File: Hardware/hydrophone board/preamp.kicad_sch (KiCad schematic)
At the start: 10 parts, among them U111 AD8541ARTZ

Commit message: changed all cap + resistors to 0805, starting filter layout
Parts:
- C111, C112, C114: footprint Capacitor_SMD:C_0603_1608Metric -> Capacitor_SMD:C_0805_2012Metric_Pad1.18x1.45mm_HandSolder
- C113: footprint Capacitor_SMD:C_0805_2012Metric -> Capacitor_SMD:C_0805_2012Metric_Pad1.18x1.45mm_HandSolder
- R111, R112, R113, R114: footprint Resistor_SMD:R_0603_1608Metric -> Resistor_SMD:R_0805_2012Metric_Pad1.20x1.40mm_HandSolder
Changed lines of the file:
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@@
       (effects (font (size 1.27 1.27)))
     )
-    (property "Footprint" "Capacitor_SMD:C_0603_1608Metric" (at 120.65 64.4652 0)
+    (property "Footprint" "Capacitor_SMD:C_0805_2012Metric_Pad1.18x1.45mm_HandSolder" (at 120.65 64.4652 0)
       (effects (font (size 1.27 1.27)) hide)
     )
@@
       (effects (font (size 1.27 1.27)) (justify left))
     )
-    (property "Footprint" "Resistor_SMD:R_0603_1608Metric" (at 96.266 108.204 90)
+    (property "Footprint" "Resistor_SMD:R_0805_2012Metric_Pad1.20x1.40mm_HandSolder" (at 96.266 108.204 90)
       (effects (font (size 1.27 1.27)) hide)
     )
@@
       (effects (font (size 1.27 1.27)))
     )
-    (property "Footprint" "Resistor_SMD:R_0603_1608Metric" (at 124.714 75.184 90)
+    (property "Footprint" "Resistor_SMD:R_0805_2012Metric_Pad1.20x1.40mm_HandSolder" (at 124.714 75.184 90)
       (effects (font (size 1.27 1.27)) hide)
     )
@@
       (effects (font (size 1.27 1.27)))
     )
-    (property "Footprint" "Capacitor_SMD:C_0805_2012Metric" (at 86.36 85.3948 0)
+    (property "Footprint" "Capacitor_SMD:C_0805_2012Metric_Pad1.18x1.45mm_HandSolder" (at 86.36 85.3948 0)
       (effects (font (size 1.27 1.27)) hide)
     )
@@
       (effects (font (size 1.27 1.27)) (justify right))
     )
-    (property "Footprint" "Capacitor_SMD:C_0603_1608Metric" (at 106.9848 116.84 0)
+    (property "Footprint" "Capacitor_SMD:C_0805_2012Metric_Pad1.18x1.45mm_HandSolder" (at 106.9848 116.84 0)
       (effects (font (size 1.27 1.27)) hide)
     )
@@
       (effects (font (size 1.27 1.27)))
     )
-    (property "Footprint" "Capacitor_SMD:C_0603_1608Metric" (at 130.81 49.8348 0)
+    (property "Footprint" "Capacitor_SMD:C_0805_2012Metric_Pad1.18x1.45mm_HandSolder" (at 130.81 49.8348 0)
       (effects (font (size 1.27 1.27)) hide)
     )
@@
       (effects (font (size 1.27 1.27)) (justify right))
     )
-    (property "Footprint" "Resistor_SMD:R_0603_1608Metric" (at 62.484 78.486 90)
+    (property "Footprint" "Resistor_SMD:R_0805_2012Metric_Pad1.20x1.40mm_HandSolder" (at 62.484 78.486 90)
       (effects (font (size 1.27 1.27)) hide)
     )
@@
       (effects (font (size 1.27 1.27)) (justify left))
     )
-    (property "Footprint" "Resistor_SMD:R_0603_1608Metric" (at 96.266 120.904 90)
-      (effects (font (size 1.27 1.27)) hide)
-    )
+    (property "Footprint" "Resistor_SMD:R_0805_2012Metric_Pad1.20x1.40mm_HandSolder" (at 96.266 120.904 90)
+      (effects (font (size 1.27 1.27)) hide)
+    )

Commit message: changed some aprts
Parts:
- removed TP?: TestPoint_Probe, Connector_PinHeader_2.54mm:PinHeader_1x01_P2.54mm_Vertical, symbol Connector:TestPoint_Probe
- added J5: Conn_01x02, Connector_PinHeader_2.54mm:PinHeader_1x02_P2.54mm_Vertical, symbol Connector_Generic:Conn_01x02
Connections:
- net GND: now also J5.1 (Pin_1)
- net OUT: now also J5.2 (Pin_2)
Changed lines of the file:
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@@
+    (stroke (width 0) (type default))
+  )
+  (wire (pts (xy 146.05 88.9) (xy 146.05 99.06))
     (stroke (width 0) (type default))
   )
@@
     (stroke (width 0) (type default))
   )
-  (wire (pts (xy 146.05 82.55) (xy 146.05 88.9))
+  (wire (pts (xy 146.05 101.6) (xy 146.05 106.68))
     (stroke (width 0) (type default))
   )
@@
     )
   )
+  (symbol (lib_id "power:GND") (at 146.05 106.68 0) (unit 1)
+    (in_bom yes) (on_board yes) (dnp no) (fields_autoplaced)
+    (property "Reference" "#PWR0205" (at 146.05 113.03 0)
+      (effects (font (size 1.27 1.27)) hide)
+    )
+    (property "Value" "GND" (at 146.05 111.76 0)
+      (effects (font (size 1.27 1.27)))
+    )
+    (property "Footprint" "" (at 146.05 106.68 0)
+      (effects (font (size 1.27 1.27)) hide)
+    )
+    (property "Datasheet" "" (at 146.05 106.68 0)
+      (effects (font (size 1.27 1.27)) hide)
+    )
+    (pin "1")
+    (instances
+      (project "hydrophone board"
+        (path "/4356d3a6-6a00-447d-897e-473f60221539/1cfbaf71-7039-4355-8fc7-d8c77f0e8058"
+          (reference "#PWR0205") (unit 1)
+        )
+        (path "/4356d3a6-6a00-447d-897e-473f60221539/f560d530-135c-40dc-9144-4f9599a30f13"
+          (reference "#PWR0252") (unit 1)
+        )
+        (path "/4356d3a6-6a00-447d-897e-473f60221539/fa1a46a1-ed86-4a84-a182-b5dbe7fc86e7"
+          (reference "#PWR0253") (unit 1)
+        )
+        (path "/4356d3a6-6a00-447d-897e-473f60221539/d3a562a3-af99-4bb5-b5fa-eb83660cffa4"
+          (reference "#PWR0254") (unit 1)
+        )
+        (path "/4356d3a6-6a00-447d-897e-473f60221539/6f981a72-1f6f-4ccf-ba7d-c5dfb70b4229"
+          (reference "#PWR0255") (unit 1)
+        )
+      )
+    )
+  )
   (symbol (lib_id "Device:C") (at 127 50.8 90) (unit 1)
     (in_bom yes) (on_board yes) (dnp no) (fields_autoplaced)
@@
         (path "/4356d3a6-6a00-447d-897e-473f60221539/6f981a72-1f6f-4ccf-ba7d-c5dfb70b4229"
           (reference "C141") (unit 1)
-        )
-      )
-    )
-  )
-  (symbol (lib_id "Connector:TestPoint_Probe") (at 146.05 82.55 0) (unit 1)
-    (in_bom yes) (on_board yes) (dnp no) (fields_autoplaced)
-    (property "Reference" "TP?" (at 149.86 80.3275 0)
-      (effects (font (size 1.27 1.27)) (justify left))
-    )
-    (property "Value" "TestPoint_Probe" (at 149.86 82.8675 0)
-      (effects (font (size 1.27 1.27)) (justify left))
-    )
-    (property "Footprint" "Connector_PinHeader_2.54mm:PinHeader_1x01_P2.54mm_Vertical" (at 151.13 82.55 0)
-      (effects (font (size 1.27 1.27)) hide)
-    )
-    (property "Datasheet" "~" (at 151.13 82.55 0)
-      (effects (font (size 1.27 1.27)) hide)
-    )
-    (pin "1")
-    (instances
-      (project "hydrophone board"
-        (path "/4356d3a6-6a00-447d-897e-473f60221539/cf9d259f-9643-49eb-8aca-1ca8b75f4d64"
-          (reference "TP?") (unit 1)
-        )
-        (path "/4356d3a6-6a00-447d-897e-473f60221539/f560d530-135c-40dc-9144-4f9599a30f13"
-          (reference "TP111") (unit 1)
-        )
-        (path "/4356d3a6-6a00-447d-897e-473f60221539/fa1a46a1-ed86-4a84-a182-b5dbe7fc86e7"
-          (reference "TP121") (unit 1)
-        )
-        (path "/4356d3a6-6a00-447d-897e-473f60221539/d3a562a3-af99-4bb5-b5fa-eb83660cffa4"
-          (reference "TP131") (unit 1)
-        )
-        (path "/4356d3a6-6a00-447d-897e-473f60221539/6f981a72-1f6f-4ccf-ba7d-c5dfb70b4229"
-          (reference "TP141") (unit 1)
         )
       )
@@
         )
       )
+    )
+  )
+  (symbol (lib_id "Connector_Generic:Conn_01x02") (at 140.97 101.6 180) (unit 1)
+    (in_bom yes) (on_board yes) (dnp no)
+    (property "Reference" "J5" (at 140.97 92.71 0)
+      (effects (font (size 1.27 1.27)))
+    )
+    (property "Value" "Conn_01x02" (at 140.97 95.25 0)
+      (effects (font (size 1.27 1.27)))
+    )
+    (property "Footprint" "Connector_PinHeader_2.54mm:PinHeader_1x02_P2.54mm_Vertical" (at 140.97 101.6 0)
+      (effects (font (size 1.27 1.27)) hide)
+    )
+    (property "Datasheet" "~" (at 140.97 101.6 0)
+      (effects (font (size 1.27 1.27)) hide)
+    )
+    (pin "1")
+    (pin "2")
+    (instances
+      (project "hydrophone board"
+        (path "/4356d3a6-6a00-447d-897e-473f60221539/1cfbaf71-7039-4355-8fc7-d8c77f0e8058"
+          (reference "J5") (unit 1)
+        )
+        (path "/4356d3a6-6a00-447d-897e-473f60221539/f560d530-135c-40dc-9144-4f9599a30f13"
+          (reference "J111") (unit 1)
+        )
+        (path "/4356d3a6-6a00-447d-897e-473f60221539/fa1a46a1-ed86-4a84-a182-b5dbe7fc86e7"
+          (reference "J121") (unit 1)
+        )
+        (path "/4356d3a6-6a00-447d-897e-473f60221539/d3a562a3-af99-4bb5-b5fa-eb83660cffa4"
+          (reference "J131") (unit 1)
+        )
+        (path "/4356d3a6-6a00-447d-897e-473f60221539/6f981a72-1f6f-4ccf-ba7d-c5dfb70b4229"
+          (reference "J141") (unit 1)
+        )
+      )

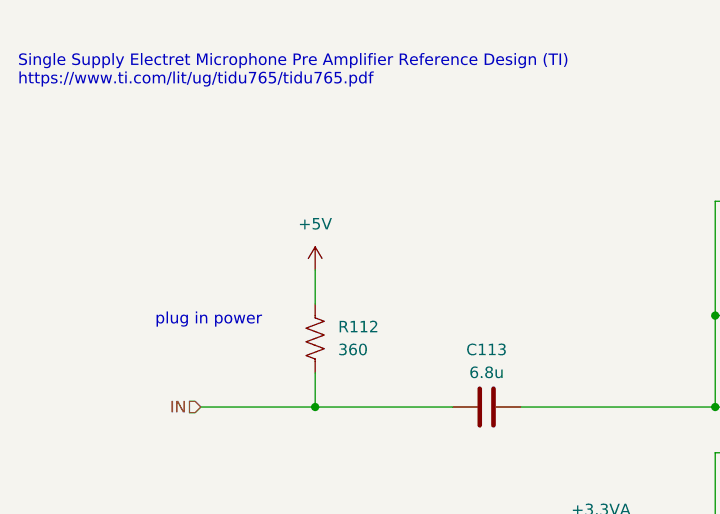
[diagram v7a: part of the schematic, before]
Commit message: power routing, changed bias voltage to 3.3
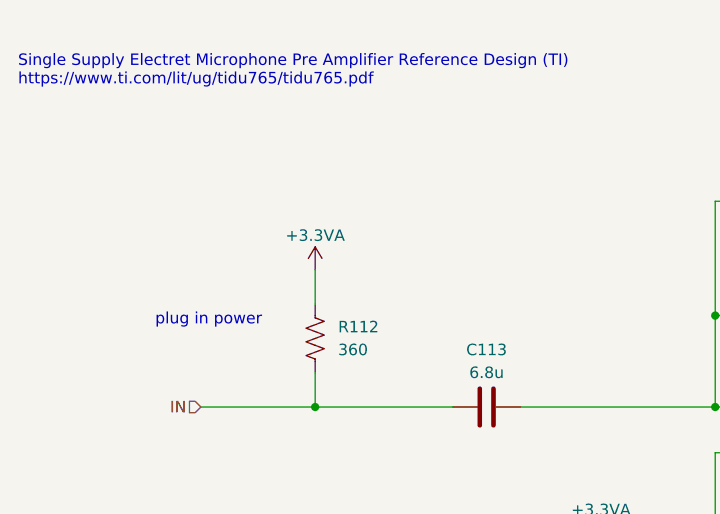
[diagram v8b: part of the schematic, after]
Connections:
- net +5V is gone; now on net +3.3VA: R112.2
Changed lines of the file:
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@@
-    )
-  )
-  (symbol (lib_id "PCM_4ms_Power-symbol:+5V") (at 63.5 71.12 0) (unit 1)
-    (in_bom yes) (on_board yes) (dnp no) (fields_autoplaced)
-    (property "Reference" "#PWR0248" (at 63.5 74.93 0)
-      (effects (font (size 1.27 1.27)) hide)
-    )
-    (property "Value" "+5V" (at 63.5 66.04 0)
-      (effects (font (size 1.27 1.27)))
-    )
-    (property "Footprint" "" (at 63.5 71.12 0)
-      (effects (font (size 1.27 1.27)) hide)
-    )
-    (property "Datasheet" "" (at 63.5 71.12 0)
-      (effects (font (size 1.27 1.27)) hide)
-    )
-    (pin "1")
-    (instances
-      (project "hydrophone board"
-        (path "/4356d3a6-6a00-447d-897e-473f60221539/f560d530-135c-40dc-9144-4f9599a30f13"
-          (reference "#PWR0248") (unit 1)
-        )
-        (path "/4356d3a6-6a00-447d-897e-473f60221539/fa1a46a1-ed86-4a84-a182-b5dbe7fc86e7"
-          (reference "#PWR0249") (unit 1)
-        )
-        (path "/4356d3a6-6a00-447d-897e-473f60221539/d3a562a3-af99-4bb5-b5fa-eb83660cffa4"
-          (reference "#PWR0250") (unit 1)
-        )
-        (path "/4356d3a6-6a00-447d-897e-473f60221539/6f981a72-1f6f-4ccf-ba7d-c5dfb70b4229"
-          (reference "#PWR0251") (unit 1)
-        )
-      )
     )
   )
@@
         )
       )
+    )
+  )
+  (symbol (lib_id "power:+3.3VA") (at 63.5 71.12 0) (unit 1)
+    (in_bom yes) (on_board yes) (dnp no) (fields_autoplaced)
+    (property "Reference" "#PWR0401" (at 63.5 74.93 0)
+      (effects (font (size 1.27 1.27)) hide)
+    )
+    (property "Value" "+3.3VA" (at 63.5 67.31 0)
+      (effects (font (size 1.27 1.27)))
+    )
+    (property "Footprint" "" (at 63.5 71.12 0)
+      (effects (font (size 1.27 1.27)) hide)
+    )
+    (property "Datasheet" "" (at 63.5 71.12 0)
+      (effects (font (size 1.27 1.27)) hide)
+    )
+    (pin "1")
+    (instances
+      (project "hydrophone board"
+        (path "/4356d3a6-6a00-447d-897e-473f60221539/c9760799-658d-4181-af96-8731ebbcaea9"
+          (reference "#PWR0401") (unit 1)
+        )
+        (path "/4356d3a6-6a00-447d-897e-473f60221539/f560d530-135c-40dc-9144-4f9599a30f13"
+          (reference "#PWR0248") (unit 1)
+        )
+        (path "/4356d3a6-6a00-447d-897e-473f60221539/fa1a46a1-ed86-4a84-a182-b5dbe7fc86e7"
+          (reference "#PWR0249") (unit 1)
+        )
+        (path "/4356d3a6-6a00-447d-897e-473f60221539/d3a562a3-af99-4bb5-b5fa-eb83660cffa4"
+          (reference "#PWR0250") (unit 1)
+        )
+        (path "/4356d3a6-6a00-447d-897e-473f60221539/6f981a72-1f6f-4ccf-ba7d-c5dfb70b4229"
+          (reference "#PWR0251") (unit 1)
+        )
+      )
